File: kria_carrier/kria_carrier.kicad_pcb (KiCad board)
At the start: 2 copper layers, 2 parts, among them J1 ADM6-60-01.5-L-4-2-A-TR, J2 ADM6-60-01.5-L-4-2-A-TR

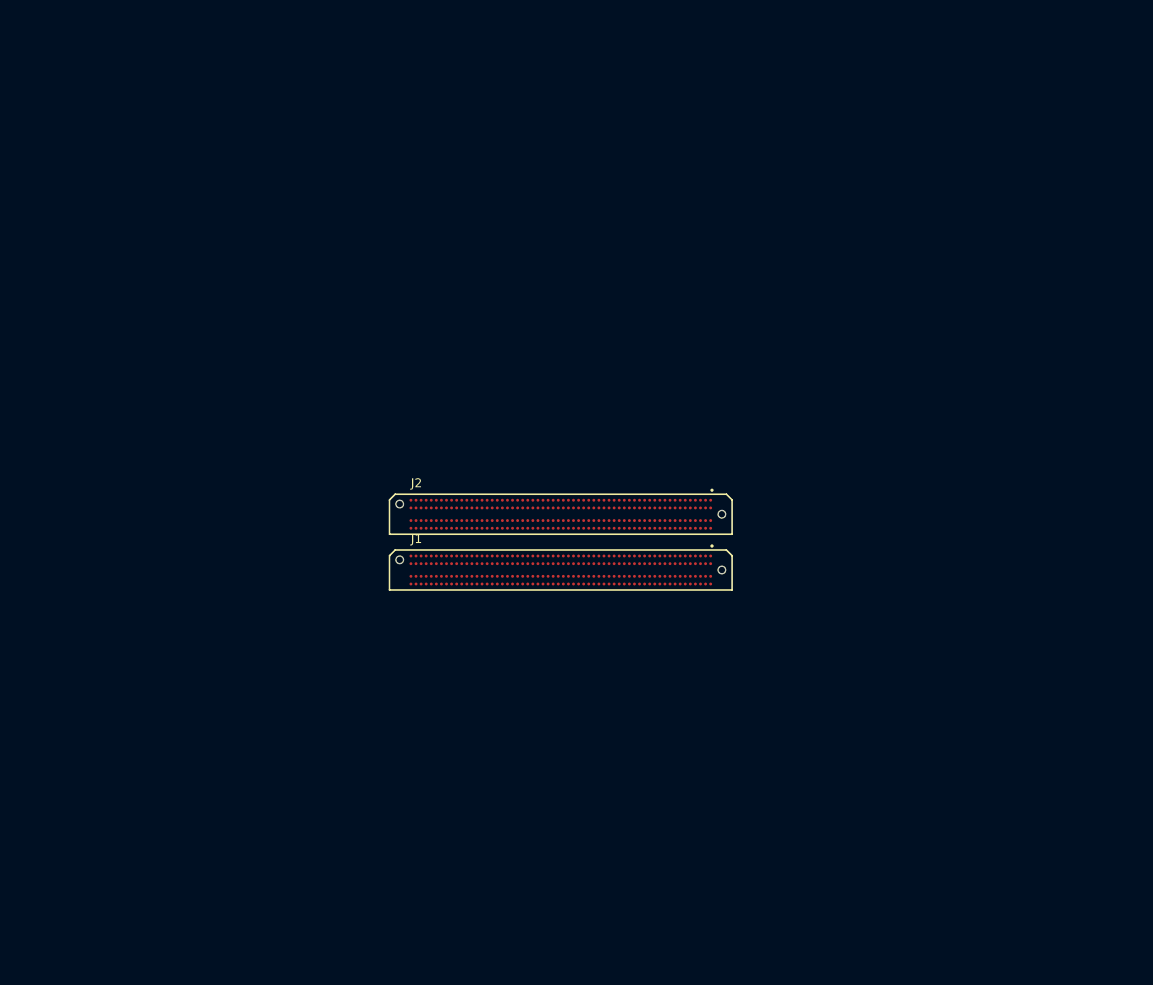
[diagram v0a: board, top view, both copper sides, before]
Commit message: library paths are messed up
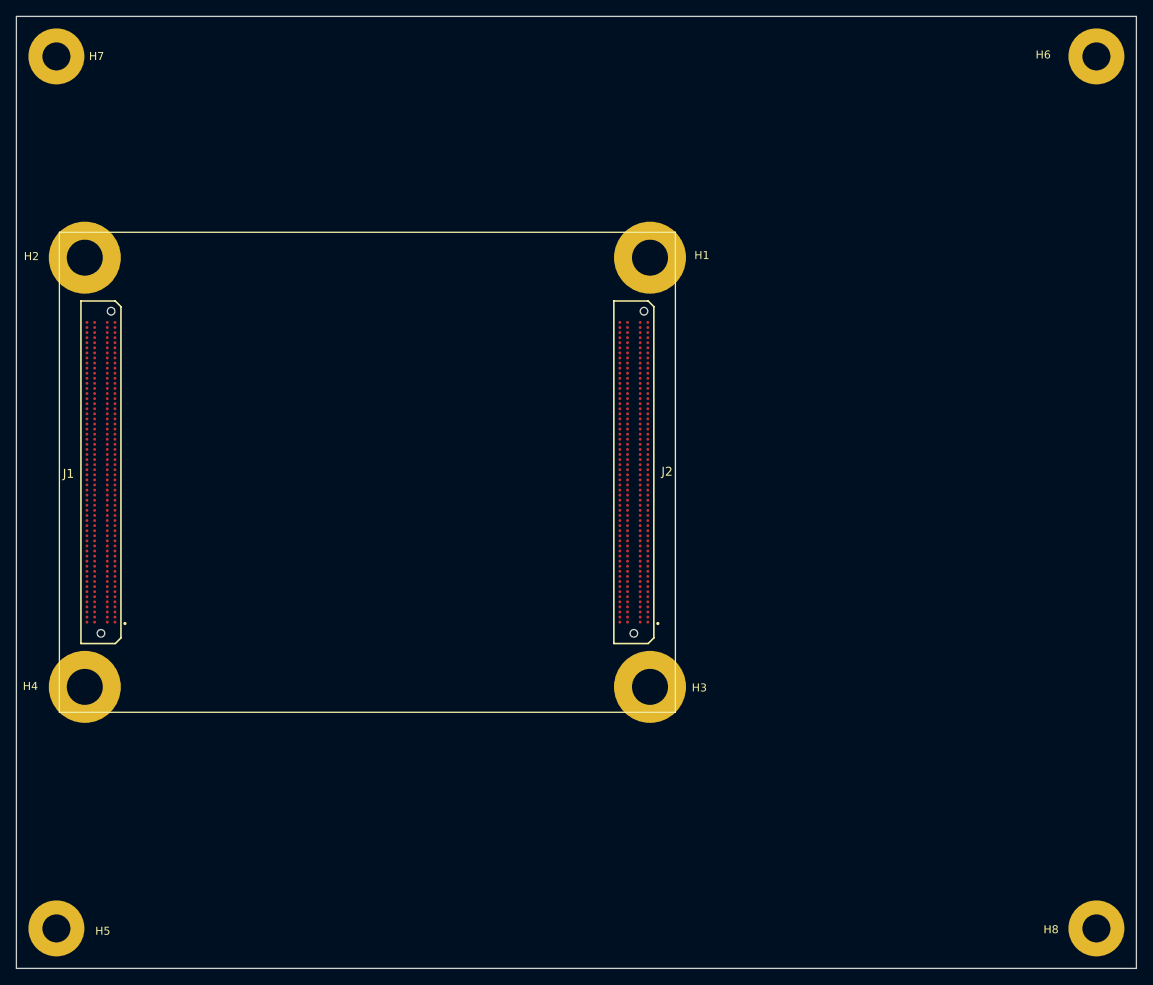
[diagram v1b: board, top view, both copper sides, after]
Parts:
- added H1: Kria_mounting_hole, MountingHole:MountingHole_4.5mm_Pad, F.Cu at (109.2, 60.2)
- added H2: Kria_mounting_hole, MountingHole:MountingHole_4.5mm_Pad, F.Cu at (38.5, 60.2)
- added H3: Kria_mounting_hole, MountingHole:MountingHole_4.5mm_Pad, F.Cu at (109.2, 113.8)
- added H4: Kria_mounting_hole, MountingHole:MountingHole_4.5mm_Pad, F.Cu at (38.5, 113.8)
- added H5: standoff_hole, MountingHole:MountingHole_3.5mm_Pad, F.Cu at (35.0, 144.0)
- added H6: standoff_hole, MountingHole:MountingHole_3.5mm_Pad, F.Cu at (165.0, 35.0)
- added H7: standoff_hole, MountingHole:MountingHole_3.5mm_Pad, F.Cu at (35.0, 35.0)
- added H8: standoff_hole, MountingHole:MountingHole_3.5mm_Pad, F.Cu at (165.0, 144.0)
- moved J1 58.8 mm to (40.6, 87.0), turned to -90 degrees
- moved J2 10.5 mm to (107.2, 87.0), turned to -90 degrees
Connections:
- J1 pad C01: (no net) -> unconnected-(J1-PadC01)
- J1 pad C02: (no net) -> unconnected-(J1-PadC02)
- J1 pad C03: (no net) -> unconnected-(J1-PadC03)
- J1 pad C04: (no net) -> unconnected-(J1-PadC04)
- J1 pad C05: (no net) -> unconnected-(J1-PadC05)
- J1 pad C06: (no net) -> unconnected-(J1-PadC06)
- J1 pad C07: (no net) -> unconnected-(J1-PadC07)
- J1 pad C08: (no net) -> unconnected-(J1-PadC08)
- J1 pad C09: (no net) -> unconnected-(J1-PadC09)
- J1 pad C10: (no net) -> unconnected-(J1-PadC10)
- J1 pad C11: (no net) -> unconnected-(J1-PadC11)
- J1 pad C12: (no net) -> unconnected-(J1-PadC12)
- J1 pad C13: (no net) -> unconnected-(J1-PadC13)
- J1 pad C14: (no net) -> unconnected-(J1-PadC14)
- J1 pad C15: (no net) -> unconnected-(J1-PadC15)
- J1 pad C16: (no net) -> unconnected-(J1-PadC16)
- J1 pad C17: (no net) -> unconnected-(J1-PadC17)
- J1 pad C18: (no net) -> unconnected-(J1-PadC18)
- J1 pad C19: (no net) -> unconnected-(J1-PadC19)
- J1 pad C20: (no net) -> unconnected-(J1-PadC20)
- J1 pad C21: (no net) -> unconnected-(J1-PadC21)
- J1 pad C22: (no net) -> unconnected-(J1-PadC22)
- J1 pad C23: (no net) -> unconnected-(J1-PadC23)
- J1 pad C24: (no net) -> unconnected-(J1-PadC24)
- J1 pad C25: (no net) -> unconnected-(J1-PadC25)
- J1 pad C26: (no net) -> unconnected-(J1-PadC26)
- J1 pad C27: (no net) -> unconnected-(J1-PadC27)
- J1 pad C28: (no net) -> unconnected-(J1-PadC28)
- J1 pad C29: (no net) -> unconnected-(J1-PadC29)
- J1 pad C30: (no net) -> unconnected-(J1-PadC30)
- J1 pad C31: (no net) -> unconnected-(J1-PadC31)
- J1 pad C32: (no net) -> unconnected-(J1-PadC32)
- J1 pad C33: (no net) -> unconnected-(J1-PadC33)
- J1 pad C34: (no net) -> unconnected-(J1-PadC34)
- J1 pad C35: (no net) -> unconnected-(J1-PadC35)
- J1 pad C36: (no net) -> unconnected-(J1-PadC36)
- J1 pad C37: (no net) -> unconnected-(J1-PadC37)
- J1 pad C38: (no net) -> unconnected-(J1-PadC38)
- J1 pad C39: (no net) -> unconnected-(J1-PadC39)
- J1 pad C40: (no net) -> unconnected-(J1-PadC40)
- J1 pad C41: (no net) -> unconnected-(J1-PadC41)
- J1 pad C42: (no net) -> unconnected-(J1-PadC42)
- J1 pad C43: (no net) -> unconnected-(J1-PadC43)
- J1 pad C44: (no net) -> unconnected-(J1-PadC44)
- J1 pad C45: (no net) -> unconnected-(J1-PadC45)
- J1 pad C46: (no net) -> unconnected-(J1-PadC46)
- J1 pad C47: (no net) -> unconnected-(J1-PadC47)
- J1 pad C48: (no net) -> unconnected-(J1-PadC48)
- J1 pad C49: (no net) -> unconnected-(J1-PadC49)
- J1 pad C50: (no net) -> unconnected-(J1-PadC50)
- J1 pad C51: (no net) -> unconnected-(J1-PadC51)
- J1 pad C52: (no net) -> unconnected-(J1-PadC52)
- J1 pad C53: (no net) -> unconnected-(J1-PadC53)
- J1 pad C54: (no net) -> unconnected-(J1-PadC54)
- J1 pad C55: (no net) -> unconnected-(J1-PadC55)
- J1 pad C56: (no net) -> unconnected-(J1-PadC56)
- J1 pad C57: (no net) -> unconnected-(J1-PadC57)
- J1 pad C58: (no net) -> unconnected-(J1-PadC58)
- J1 pad C59: (no net) -> unconnected-(J1-PadC59)
- J1 pad C60: (no net) -> unconnected-(J1-PadC60)
- J1 pad D01: (no net) -> unconnected-(J1-PadD01)
- J1 pad D02: (no net) -> unconnected-(J1-PadD02)
- J1 pad D03: (no net) -> unconnected-(J1-PadD03)
- J1 pad D04: (no net) -> unconnected-(J1-PadD04)
- J1 pad D05: (no net) -> unconnected-(J1-PadD05)
- J1 pad D06: (no net) -> unconnected-(J1-PadD06)
- J1 pad D07: (no net) -> unconnected-(J1-PadD07)
- J1 pad D08: (no net) -> unconnected-(J1-PadD08)
- J1 pad D09: (no net) -> unconnected-(J1-PadD09)
- J1 pad D10: (no net) -> unconnected-(J1-PadD10)
- J1 pad D11: (no net) -> unconnected-(J1-PadD11)
- J1 pad D12: (no net) -> unconnected-(J1-PadD12)
- J1 pad D13: (no net) -> unconnected-(J1-PadD13)
- J1 pad D14: (no net) -> unconnected-(J1-PadD14)
- J1 pad D15: (no net) -> unconnected-(J1-PadD15)
- J1 pad D16: (no net) -> unconnected-(J1-PadD16)
- J1 pad D17: (no net) -> unconnected-(J1-PadD17)
- J1 pad D18: (no net) -> unconnected-(J1-PadD18)
- J1 pad D19: (no net) -> unconnected-(J1-PadD19)
- J1 pad D20: (no net) -> unconnected-(J1-PadD20)
- J1 pad D21: (no net) -> unconnected-(J1-PadD21)
- J1 pad D22: (no net) -> unconnected-(J1-PadD22)
- J1 pad D23: (no net) -> unconnected-(J1-PadD23)
- J1 pad D24: (no net) -> unconnected-(J1-PadD24)
- J1 pad D25: (no net) -> unconnected-(J1-PadD25)
- J1 pad D26: (no net) -> unconnected-(J1-PadD26)
- J1 pad D27: (no net) -> unconnected-(J1-PadD27)
- J1 pad D28: (no net) -> unconnected-(J1-PadD28)
- J1 pad D29: (no net) -> unconnected-(J1-PadD29)
- J1 pad D30: (no net) -> unconnected-(J1-PadD30)
- J1 pad D31: (no net) -> unconnected-(J1-PadD31)
- J1 pad D32: (no net) -> unconnected-(J1-PadD32)
- J1 pad D33: (no net) -> unconnected-(J1-PadD33)
- J1 pad D34: (no net) -> unconnected-(J1-PadD34)
- J1 pad D35: (no net) -> unconnected-(J1-PadD35)
- J1 pad D36: (no net) -> unconnected-(J1-PadD36)
- J1 pad D37: (no net) -> unconnected-(J1-PadD37)
- J1 pad D38: (no net) -> unconnected-(J1-PadD38)
- J1 pad D39: (no net) -> unconnected-(J1-PadD39)
- J1 pad D40: (no net) -> unconnected-(J1-PadD40)
- J1 pad D41: (no net) -> unconnected-(J1-PadD41)
- J1 pad D42: (no net) -> unconnected-(J1-PadD42)
- J1 pad D43: (no net) -> unconnected-(J1-PadD43)
- J1 pad D44: (no net) -> unconnected-(J1-PadD44)
- J1 pad D45: (no net) -> unconnected-(J1-PadD45)
- J1 pad D46: (no net) -> unconnected-(J1-PadD46)
- J1 pad D47: (no net) -> unconnected-(J1-PadD47)
- J1 pad D48: (no net) -> unconnected-(J1-PadD48)
- J1 pad D49: (no net) -> unconnected-(J1-PadD49)
- J1 pad D50: (no net) -> unconnected-(J1-PadD50)
- J1 pad D51: (no net) -> unconnected-(J1-PadD51)
- J1 pad D52: (no net) -> unconnected-(J1-PadD52)
- J1 pad D53: (no net) -> unconnected-(J1-PadD53)
- J1 pad D54: (no net) -> unconnected-(J1-PadD54)
- J1 pad D55: (no net) -> unconnected-(J1-PadD55)
- J1 pad D56: (no net) -> unconnected-(J1-PadD56)
- J1 pad D57: (no net) -> unconnected-(J1-PadD57)
- J1 pad D58: (no net) -> unconnected-(J1-PadD58)
- J1 pad D59: (no net) -> unconnected-(J1-PadD59)
- J1 pad D60: (no net) -> unconnected-(J1-PadD60)
- J2 pad C01: (no net) -> unconnected-(J2-PadC01)
- J2 pad C02: (no net) -> unconnected-(J2-PadC02)
- J2 pad C03: (no net) -> unconnected-(J2-PadC03)
- J2 pad C04: (no net) -> unconnected-(J2-PadC04)
- J2 pad C05: (no net) -> unconnected-(J2-PadC05)
- J2 pad C06: (no net) -> unconnected-(J2-PadC06)
- J2 pad C07: (no net) -> unconnected-(J2-PadC07)
- J2 pad C08: (no net) -> unconnected-(J2-PadC08)
- J2 pad C09: (no net) -> unconnected-(J2-PadC09)
- J2 pad C10: (no net) -> unconnected-(J2-PadC10)
- J2 pad C11: (no net) -> unconnected-(J2-PadC11)
- J2 pad C12: (no net) -> unconnected-(J2-PadC12)
- J2 pad C13: (no net) -> unconnected-(J2-PadC13)
- J2 pad C14: (no net) -> unconnected-(J2-PadC14)
- J2 pad C15: (no net) -> unconnected-(J2-PadC15)
- J2 pad C16: (no net) -> unconnected-(J2-PadC16)
- J2 pad C17: (no net) -> unconnected-(J2-PadC17)
- J2 pad C18: (no net) -> unconnected-(J2-PadC18)
- J2 pad C19: (no net) -> unconnected-(J2-PadC19)
- J2 pad C20: (no net) -> unconnected-(J2-PadC20)
- J2 pad C21: (no net) -> unconnected-(J2-PadC21)
- J2 pad C22: (no net) -> unconnected-(J2-PadC22)
- J2 pad C23: (no net) -> unconnected-(J2-PadC23)
- J2 pad C24: (no net) -> unconnected-(J2-PadC24)
- J2 pad C25: (no net) -> unconnected-(J2-PadC25)
- J2 pad C26: (no net) -> unconnected-(J2-PadC26)
- J2 pad C27: (no net) -> unconnected-(J2-PadC27)
- J2 pad C28: (no net) -> unconnected-(J2-PadC28)
- J2 pad C29: (no net) -> unconnected-(J2-PadC29)
- J2 pad C30: (no net) -> unconnected-(J2-PadC30)
- J2 pad C31: (no net) -> unconnected-(J2-PadC31)
- J2 pad C32: (no net) -> unconnected-(J2-PadC32)
- J2 pad C33: (no net) -> unconnected-(J2-PadC33)
- J2 pad C34: (no net) -> unconnected-(J2-PadC34)
- J2 pad C35: (no net) -> unconnected-(J2-PadC35)
- J2 pad C36: (no net) -> unconnected-(J2-PadC36)
- J2 pad C37: (no net) -> unconnected-(J2-PadC37)
- J2 pad C38: (no net) -> unconnected-(J2-PadC38)
- J2 pad C39: (no net) -> unconnected-(J2-PadC39)
- J2 pad C40: (no net) -> unconnected-(J2-PadC40)
- J2 pad C41: (no net) -> unconnected-(J2-PadC41)
- J2 pad C42: (no net) -> unconnected-(J2-PadC42)
- J2 pad C43: (no net) -> unconnected-(J2-PadC43)
- J2 pad C44: (no net) -> unconnected-(J2-PadC44)
- J2 pad C45: (no net) -> unconnected-(J2-PadC45)
- J2 pad C46: (no net) -> unconnected-(J2-PadC46)
- J2 pad C47: (no net) -> unconnected-(J2-PadC47)
- J2 pad C48: (no net) -> unconnected-(J2-PadC48)
- J2 pad C49: (no net) -> unconnected-(J2-PadC49)
- J2 pad C50: (no net) -> unconnected-(J2-PadC50)
- J2 pad C51: (no net) -> unconnected-(J2-PadC51)
- J2 pad C52: (no net) -> unconnected-(J2-PadC52)
- J2 pad C53: (no net) -> unconnected-(J2-PadC53)
- J2 pad C54: (no net) -> unconnected-(J2-PadC54)
- J2 pad C55: (no net) -> unconnected-(J2-PadC55)
- J2 pad C56: (no net) -> unconnected-(J2-PadC56)
- J2 pad C57: (no net) -> unconnected-(J2-PadC57)
- J2 pad C58: (no net) -> unconnected-(J2-PadC58)
- J2 pad C59: (no net) -> unconnected-(J2-PadC59)
- J2 pad C60: (no net) -> unconnected-(J2-PadC60)
- J2 pad D01: (no net) -> unconnected-(J2-PadD01)
- J2 pad D02: (no net) -> unconnected-(J2-PadD02)
- J2 pad D03: (no net) -> unconnected-(J2-PadD03)
- J2 pad D04: (no net) -> unconnected-(J2-PadD04)
- J2 pad D05: (no net) -> unconnected-(J2-PadD05)
- J2 pad D06: (no net) -> unconnected-(J2-PadD06)
- J2 pad D07: (no net) -> unconnected-(J2-PadD07)
- J2 pad D08: (no net) -> unconnected-(J2-PadD08)
- J2 pad D09: (no net) -> unconnected-(J2-PadD09)
- J2 pad D10: (no net) -> unconnected-(J2-PadD10)
- J2 pad D11: (no net) -> unconnected-(J2-PadD11)
- J2 pad D12: (no net) -> unconnected-(J2-PadD12)
- J2 pad D13: (no net) -> unconnected-(J2-PadD13)
- J2 pad D14: (no net) -> unconnected-(J2-PadD14)
- J2 pad D15: (no net) -> unconnected-(J2-PadD15)
- J2 pad D16: (no net) -> unconnected-(J2-PadD16)
- J2 pad D17: (no net) -> unconnected-(J2-PadD17)
- J2 pad D18: (no net) -> unconnected-(J2-PadD18)
- J2 pad D19: (no net) -> unconnected-(J2-PadD19)
- J2 pad D20: (no net) -> unconnected-(J2-PadD20)
- J2 pad D21: (no net) -> unconnected-(J2-PadD21)
- J2 pad D22: (no net) -> unconnected-(J2-PadD22)
- J2 pad D23: (no net) -> unconnected-(J2-PadD23)
- J2 pad D24: (no net) -> unconnected-(J2-PadD24)
- J2 pad D25: (no net) -> unconnected-(J2-PadD25)
- J2 pad D26: (no net) -> unconnected-(J2-PadD26)
- J2 pad D27: (no net) -> unconnected-(J2-PadD27)
- J2 pad D28: (no net) -> unconnected-(J2-PadD28)
- J2 pad D29: (no net) -> unconnected-(J2-PadD29)
- J2 pad D30: (no net) -> unconnected-(J2-PadD30)
- J2 pad D31: (no net) -> unconnected-(J2-PadD31)
- J2 pad D32: (no net) -> unconnected-(J2-PadD32)
- J2 pad D33: (no net) -> unconnected-(J2-PadD33)
- J2 pad D34: (no net) -> unconnected-(J2-PadD34)
- J2 pad D35: (no net) -> unconnected-(J2-PadD35)
- J2 pad D36: (no net) -> unconnected-(J2-PadD36)
- J2 pad D37: (no net) -> unconnected-(J2-PadD37)
- J2 pad D38: (no net) -> unconnected-(J2-PadD38)
- J2 pad D39: (no net) -> unconnected-(J2-PadD39)
- J2 pad D40: (no net) -> unconnected-(J2-PadD40)
- J2 pad D41: (no net) -> unconnected-(J2-PadD41)
- J2 pad D42: (no net) -> unconnected-(J2-PadD42)
- J2 pad D43: (no net) -> unconnected-(J2-PadD43)
- J2 pad D44: (no net) -> unconnected-(J2-PadD44)
- J2 pad D45: (no net) -> unconnected-(J2-PadD45)
- J2 pad D46: (no net) -> unconnected-(J2-PadD46)
- J2 pad D47: (no net) -> unconnected-(J2-PadD47)
- J2 pad D48: (no net) -> unconnected-(J2-PadD48)
- J2 pad D49: (no net) -> unconnected-(J2-PadD49)
- J2 pad D50: (no net) -> unconnected-(J2-PadD50)
- J2 pad D51: (no net) -> unconnected-(J2-PadD51)
- J2 pad D52: (no net) -> unconnected-(J2-PadD52)
- J2 pad D53: (no net) -> unconnected-(J2-PadD53)
- J2 pad D54: (no net) -> unconnected-(J2-PadD54)
- J2 pad D55: (no net) -> unconnected-(J2-PadD55)
- J2 pad D56: (no net) -> unconnected-(J2-PadD56)
- J2 pad D57: (no net) -> unconnected-(J2-PadD57)
- J2 pad D58: (no net) -> unconnected-(J2-PadD58)
- J2 pad D59: (no net) -> unconnected-(J2-PadD59)
- J2 pad D60: (no net) -> unconnected-(J2-PadD60)
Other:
- board outline added: 140 x 119 mm

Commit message: working on the power connections to the kria connectors. That connector will be tight to escape.
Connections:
- H1 pad 1: unconnected-(H1-Pad1) -> GND
- H2 pad 1: unconnected-(H2-Pad1) -> GND
- H3 pad 1: unconnected-(H3-Pad1) -> GND
- H4 pad 1: unconnected-(H4-Pad1) -> GND
- H5 pad 1: unconnected-(H5-Pad1) -> GND
- H6 pad 1: unconnected-(H6-Pad1) -> GND
- H7 pad 1: unconnected-(H7-Pad1) -> GND
- H8 pad 1: unconnected-(H8-Pad1) -> GND
- J1 pad A02: unconnected-(J1-PadA02) -> GND
- J1 pad A05: unconnected-(J1-PadA05) -> GND
- J1 pad A08: unconnected-(J1-PadA08) -> GND
- J1 pad A11: unconnected-(J1-PadA11) -> GND
- J1 pad A14: unconnected-(J1-PadA14) -> GND
- J1 pad A18: unconnected-(J1-PadA18) -> GND
- J1 pad A21: unconnected-(J1-PadA21) -> GND
- J1 pad A26: unconnected-(J1-PadA26) -> GND
- J1 pad A33: unconnected-(J1-PadA33) -> GND
- J1 pad A37: unconnected-(J1-PadA37) -> GND
- J1 pad A41: unconnected-(J1-PadA41) -> GND
- J1 pad A45: unconnected-(J1-PadA45) -> GND
- J1 pad A46: unconnected-(J1-PadA46) -> GND
- J1 pad A49: unconnected-(J1-PadA49) -> GND
- J1 pad A50: unconnected-(J1-PadA50) -> GND
- J1 pad A53: unconnected-(J1-PadA53) -> GND
- J1 pad A54: unconnected-(J1-PadA54) -> GND
- J1 pad A57: unconnected-(J1-PadA57) -> GND
- J1 pad A58: unconnected-(J1-PadA58) -> GND
- J1 pad B03: unconnected-(J1-PadB03) -> GND
- J1 pad B06: unconnected-(J1-PadB06) -> GND
- J1 pad B08: unconnected-(J1-PadB08) -> GND
- J1 pad B12: unconnected-(J1-PadB12) -> GND
- J1 pad B15: unconnected-(J1-PadB15) -> GND
- J1 pad B19: unconnected-(J1-PadB19) -> GND
- J1 pad B23: unconnected-(J1-PadB23) -> GND
- J1 pad B27: unconnected-(J1-PadB27) -> GND
- J1 pad B31: unconnected-(J1-PadB31) -> GND
- J1 pad B35: unconnected-(J1-PadB35) -> GND
- J1 pad B39: unconnected-(J1-PadB39) -> GND
- J1 pad B43: unconnected-(J1-PadB43) -> GND
- J1 pad B47: unconnected-(J1-PadB47) -> GND
- J1 pad B48: unconnected-(J1-PadB48) -> GND
- J1 pad B51: unconnected-(J1-PadB51) -> GND
- J1 pad B52: unconnected-(J1-PadB52) -> GND
- J1 pad B55: unconnected-(J1-PadB55) -> GND
- J1 pad B56: unconnected-(J1-PadB56) -> GND
- J1 pad B59: unconnected-(J1-PadB59) -> GND
- J1 pad C01: unconnected-(J1-PadC01) -> GND
- J1 pad C05: unconnected-(J1-PadC05) -> GND
- J1 pad C08: unconnected-(J1-PadC08) -> GND
- J1 pad C11: unconnected-(J1-PadC11) -> GND
- J1 pad C14: unconnected-(J1-PadC14) -> GND
- J1 pad C17: unconnected-(J1-PadC17) -> GND
- J1 pad C21: unconnected-(J1-PadC21) -> GND
- J1 pad C25: unconnected-(J1-PadC25) -> GND
- J1 pad C29: unconnected-(J1-PadC29) -> GND
- J1 pad C33: unconnected-(J1-PadC33) -> GND
- J1 pad C37: unconnected-(J1-PadC37) -> GND
- J1 pad C41: unconnected-(J1-PadC41) -> GND
- J1 pad C46: unconnected-(J1-PadC46) -> GND
- J1 pad C49: unconnected-(J1-PadC49) -> GND
- J1 pad C50: unconnected-(J1-PadC50) -> GND
- J1 pad C53: unconnected-(J1-PadC53) -> GND
- J1 pad C54: unconnected-(J1-PadC54) -> GND
- J1 pad C57: unconnected-(J1-PadC57) -> GND
- J1 pad C58: unconnected-(J1-PadC58) -> GND
- J1 pad D03: unconnected-(J1-PadD03) -> GND
- J1 pad D06: unconnected-(J1-PadD06) -> GND
- J1 pad D09: unconnected-(J1-PadD09) -> GND
- J1 pad D12: unconnected-(J1-PadD12) -> GND
- J1 pad D15: unconnected-(J1-PadD15) -> GND
- J1 pad D19: unconnected-(J1-PadD19) -> GND
- J1 pad D23: unconnected-(J1-PadD23) -> GND
- J1 pad D27: unconnected-(J1-PadD27) -> GND
- J1 pad D31: unconnected-(J1-PadD31) -> GND
- J1 pad D35: unconnected-(J1-PadD35) -> GND
- J1 pad D39: unconnected-(J1-PadD39) -> GND
- J1 pad D43: unconnected-(J1-PadD43) -> GND
- J1 pad D47: unconnected-(J1-PadD47) -> GND
- J1 pad D48: unconnected-(J1-PadD48) -> GND
- J1 pad D51: unconnected-(J1-PadD51) -> GND
- J1 pad D52: unconnected-(J1-PadD52) -> GND
- J1 pad D55: unconnected-(J1-PadD55) -> GND
- J1 pad D56: unconnected-(J1-PadD56) -> GND
- J1 pad D59: unconnected-(J1-PadD59) -> GND
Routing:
- added copper zone on In1.Cu, net GND
- added copper zone on In4.Cu, net GND
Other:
- copper layers 2 -> 6

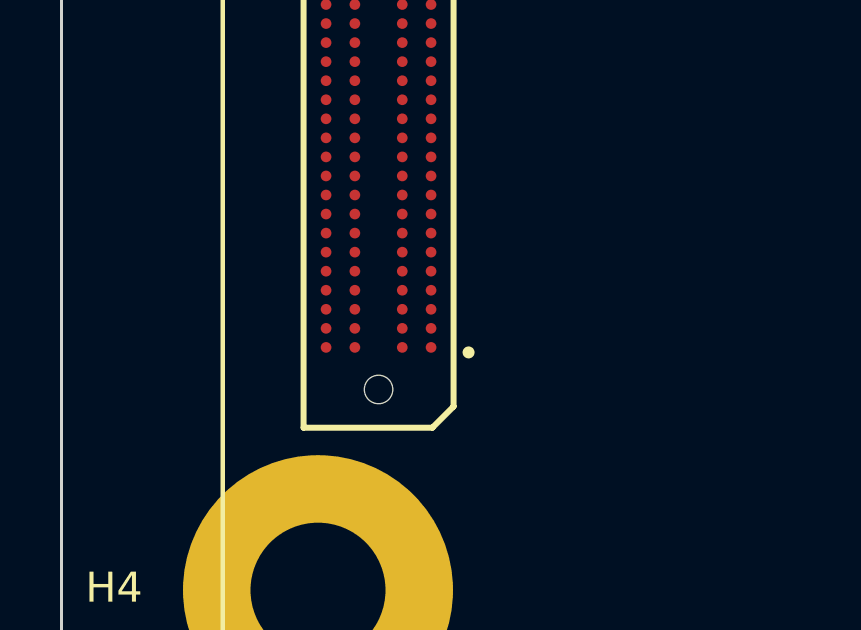
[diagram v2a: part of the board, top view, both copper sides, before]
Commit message: starting to work power and ground planes, also kria connector fanout
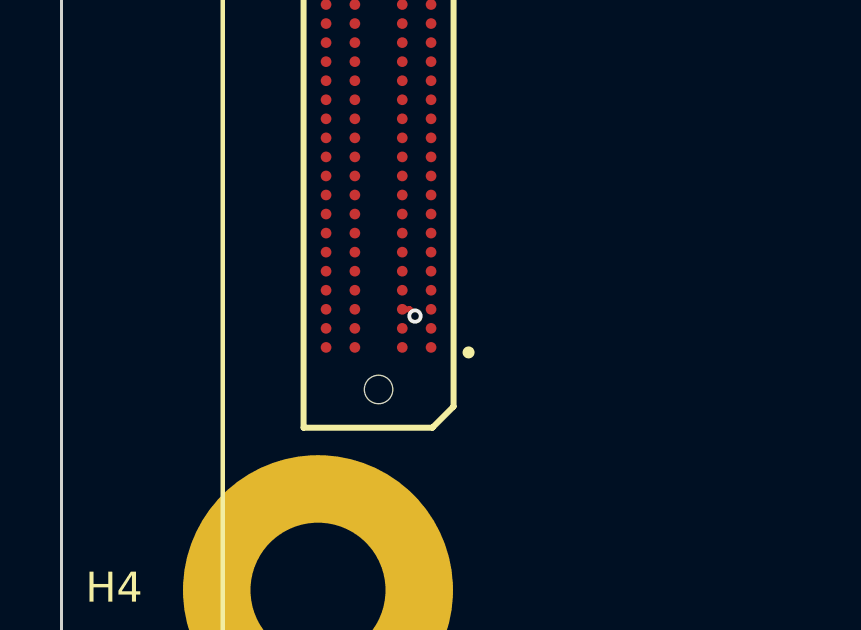
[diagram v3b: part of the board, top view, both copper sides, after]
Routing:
- net GND: track 0.00 -> 0.55 mm, vias 0 -> 1
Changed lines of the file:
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@@
 (kicad_pcb (version 20211014) (generator pcbnew)
   (general
-    (thickness 7.78)
+    (thickness 1.580264)
   )
   (paper "A")
@@
       (layer "F.Mask" (type "Top Solder Mask") (thickness 0.01))
       (layer "F.Cu" (type "copper") (thickness 0.035))
-      (layer "dielectric 1" (type "core") (thickness 1.51) (material "FR4") (epsilon_r 4.5) (loss_tangent 0.02))
+      (layer "dielectric 1" (type "core") (thickness 0.110744) (material "FR4") (epsilon_r 3.23) (loss_tangent 0.02))
       (layer "In1.Cu" (type "copper") (thickness 0.035))
-      (layer "dielectric 2" (type "prepreg") (thickness 1.51) (material "FR4") (epsilon_r 4.5) (loss_tangent 0.02))
+      (layer "dielectric 2" (type "prepreg") (thickness 0.1016) (material "FR4") (epsilon_r 3.66) (loss_tangent 0.02))
       (layer "In2.Cu" (type "copper") (thickness 0.035))
-      (layer "dielectric 3" (type "core") (thickness 1.51) (material "FR4") (epsilon_r 4.5) (loss_tangent 0.02))
+      (layer "dielectric 3" (type "core") (thickness 0.925576) (material "FR4") (epsilon_r 3.66) (loss_tangent 0.02))
       (layer "In3.Cu" (type "copper") (thickness 0.035))
-      (layer "dielectric 4" (type "prepreg") (thickness 1.51) (material "FR4") (epsilon_r 4.5) (loss_tangent 0.02))
+      (layer "dielectric 4" (type "prepreg") (thickness 0.1016) (material "FR4") (epsilon_r 3.66) (loss_tangent 0.02))
       (layer "In4.Cu" (type "copper") (thickness 0.035))
-      (layer "dielectric 5" (type "core") (thickness 1.51) (material "FR4") (epsilon_r 4.5) (loss_tangent 0.02))
+      (layer "dielectric 5" (type "core") (thickness 0.110744) (material "FR4") (epsilon_r 3.23) (loss_tangent 0.02))
       (layer "B.Cu" (type "copper") (thickness 0.035))
       (layer "B.Mask" (type "Bottom Solder Mask") (thickness 0.01))
@@
   (gr_rect locked (start 35.375 56.985) (end 112.375 116.985) (layer "F.SilkS") (width 0.15) (fill none))
   (gr_rect locked (start 30 30) (end 170 149) (layer "Edge.Cuts") (width 0.1) (fill none))
+  (segment (start 41.359 104.4475) (end 41.6079 104.4475) (width 0.2) (layer "F.Cu") (net 405))
+  (segment (start 41.6079 104.4475) (end 41.783 104.6226) (width 0.2) (layer "F.Cu") (net 405))
+  (segment (start 41.783 104.6226) (end 41.783 104.6734) (width 0.2) (layer "F.Cu") (net 405))
+  (via (at 41.783 104.6734) (size 0.508) (drill 0.254) (layers "F.Cu" "B.Cu") (net 405))
   (zone (net 405) (net_name "GND") (layer "In1.Cu") (hatch edge 0.508)
     (connect_pads (clearance 0.508))
     (min_thickness 0.254) (filled_areas_thickness no)
-    (fill (thermal_gap 0.508) (thermal_bridge_width 0.508))
+    (fill yes (thermal_gap 0.508) (thermal_bridge_width 0.508))
     (polygon
       (pts
@@
     (connect_pads (clearance 0.508))
     (min_thickness 0.254) (filled_areas_thickness no)
-    (fill (thermal_gap 0.508) (thermal_bridge_width 0.508))
+    (fill yes (thermal_gap 0.508) (thermal_bridge_width 0.508))
     (polygon
       (pts
